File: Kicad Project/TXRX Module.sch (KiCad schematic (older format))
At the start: 16 parts, among them U10 GALI-2+, U11 BandpassFilter, U13 Antenna111, U14 Antenna111, U9 LEE-39+

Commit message: PCB LAYOUT update
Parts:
- gave numbers to parts that had none: 2
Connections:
- net labels added: PowerSplitter, RFIN
- net labels removed: receive_out, transmit_in
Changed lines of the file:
@@
 Text Notes 6500 5800 0    60   ~ 0
 Hello world
-Text HLabel 2350 2650 0    60   Input ~ 0
-transmit_in
-Text HLabel 2350 4800 0    60   Input ~ 0
-receive_out
 $Comp
 L C C11
@@
 $EndComp
 $Comp
-L GND #PWR015
+L GND #PWR011
 U 1 1 59FFE5A2
 P 2350 4350
-F 0 "#PWR015" H 2350 4100 50  0001 C CNN
+F 0 "#PWR011" H 2350 4100 50  0001 C CNN
 F 1 "GND" H 2350 4200 50  0000 C CNN
 F 2 "" H 2350 4350 50  0001 C CNN
@@
 $EndComp
 $Comp
-L GND #PWR016
+L GND #PWR012
 U 1 1 59FFE5D4
 P 3850 5400
-F 0 "#PWR016" H 3850 5150 50  0001 C CNN
+F 0 "#PWR012" H 3850 5150 50  0001 C CNN
 F 1 "GND" H 3850 5250 50  0000 C CNN
 F 2 "" H 3850 5400 50  0001 C CNN
@@
 $EndComp
 $Comp
-L GND #PWR017
+L GND #PWR013
 U 1 1 59FFE606
 P 4050 3200
-F 0 "#PWR017" H 4050 2950 50  0001 C CNN
+F 0 "#PWR013" H 4050 2950 50  0001 C CNN
 F 1 "GND" H 4050 3050 50  0000 C CNN
 F 2 "" H 4050 3200 50  0001 C CNN
@@
 $EndComp
 $Comp
-L GND #PWR018
+L GND #PWR014
 U 1 1 59FFE638
 P 5450 2200
-F 0 "#PWR018" H 5450 1950 50  0001 C CNN
+F 0 "#PWR014" H 5450 1950 50  0001 C CNN
 F 1 "GND" H 5450 2050 50  0000 C CNN
 F 2 "" H 5450 2200 50  0001 C CNN
@@
 	2350 4800 2550 4800
 $Comp
-L +9V #PWR?
+L +9V #PWR015
 U 1 1 5A01141C
 P 5750 1500
-F 0 "#PWR?" H 5750 1350 50  0001 C CNN
+F 0 "#PWR015" H 5750 1350 50  0001 C CNN
 F 1 "+9V" H 5750 1640 50  0000 C CNN
 F 2 "" H 5750 1500 50  0001 C CNN
@@
 $EndComp
 $Comp
-L +9V #PWR?
+L +9V #PWR016
 U 1 1 5A0114D0
 P 3700 3800
-F 0 "#PWR?" H 3700 3650 50  0001 C CNN
+F 0 "#PWR016" H 3700 3650 50  0001 C CNN
 F 1 "+9V" H 3700 3940 50  0000 C CNN
 F 2 "" H 3700 3800 50  0001 C CNN
@@
 	5750 1650 5750 1500
 $Comp
-L BandpassFilterRx U?
+L BandpassFilterRx U3
 U 1 1 5A012078
 P 6700 5750
-F 0 "U?" H 6700 5750 60  0000 C CNN
+F 0 "U3" H 6700 5750 60  0000 C CNN
 F 1 "BandpassFilterRx" H 7250 6100 60  0000 C CNN
 F 2 "" H 6700 5750 60  0001 C CNN
@@
 $EndComp
 $Comp
-L C C?
+L C C4
 U 1 1 5A012959
 P 4800 4800
-F 0 "C?" H 4825 4900 50  0000 L CNN
+F 0 "C4" H 4825 4900 50  0000 L CNN
 F 1 "150p" H 4825 4700 50  0000 L CNN
 F 2 "" H 4838 4650 50  0001 C CNN
@@
 Wire Wire Line
 	4650 4800 4550 4800
+Text GLabel 2350 2650 0    60   Input ~ 0
+PowerSplitter
+Text GLabel 2350 4800 0    60   Input ~ 0
+RFIN
 $EndSCHEMATC

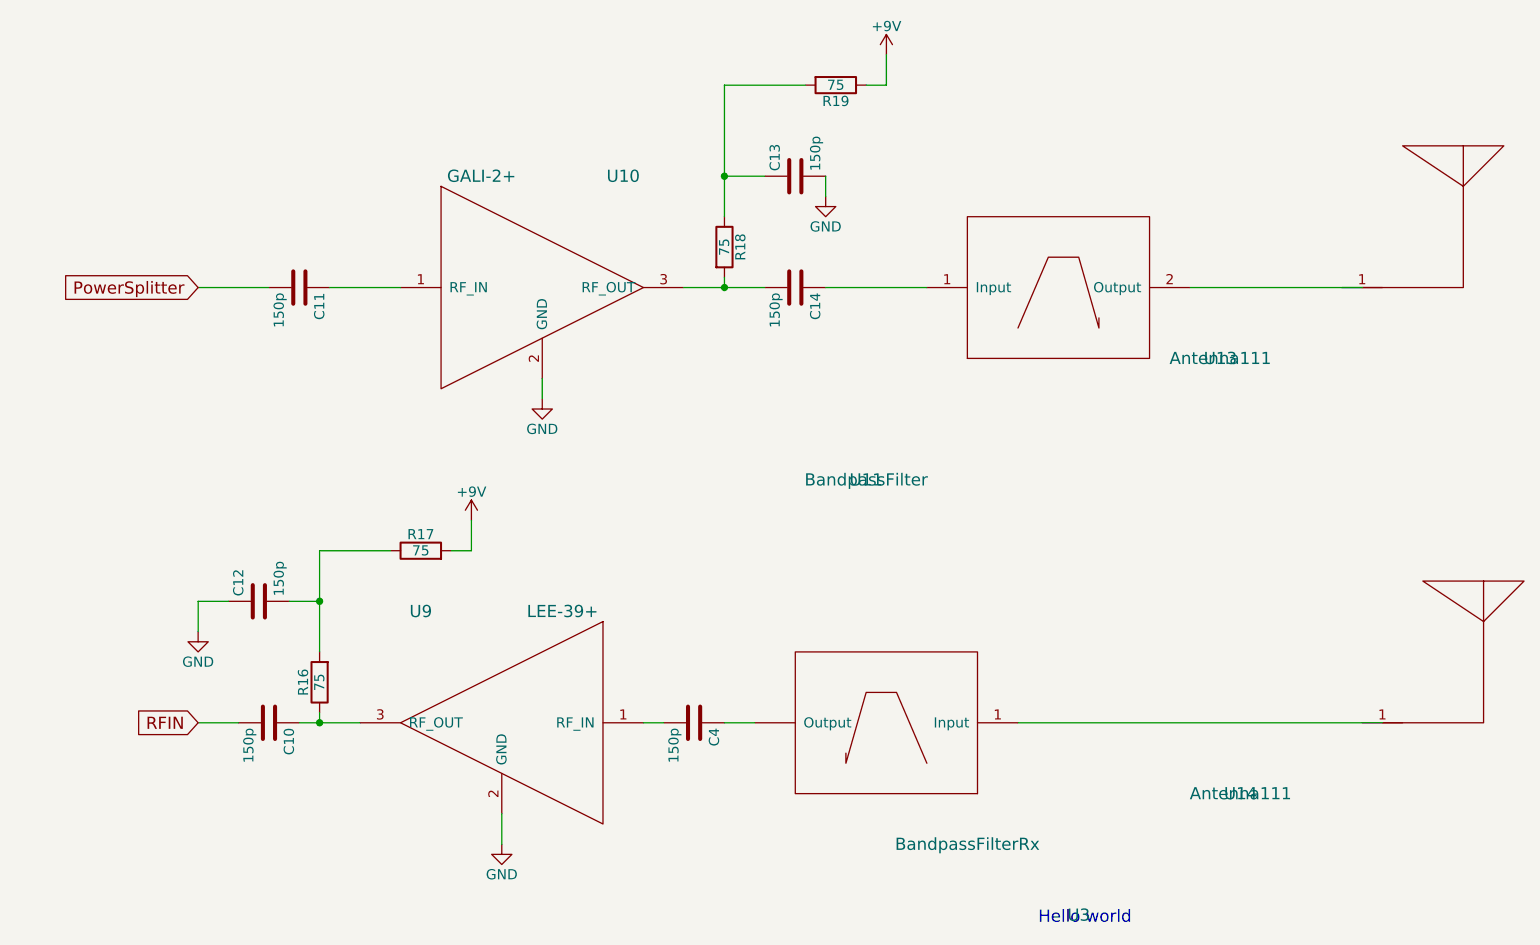
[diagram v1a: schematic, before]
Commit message: Added Filters to PCB
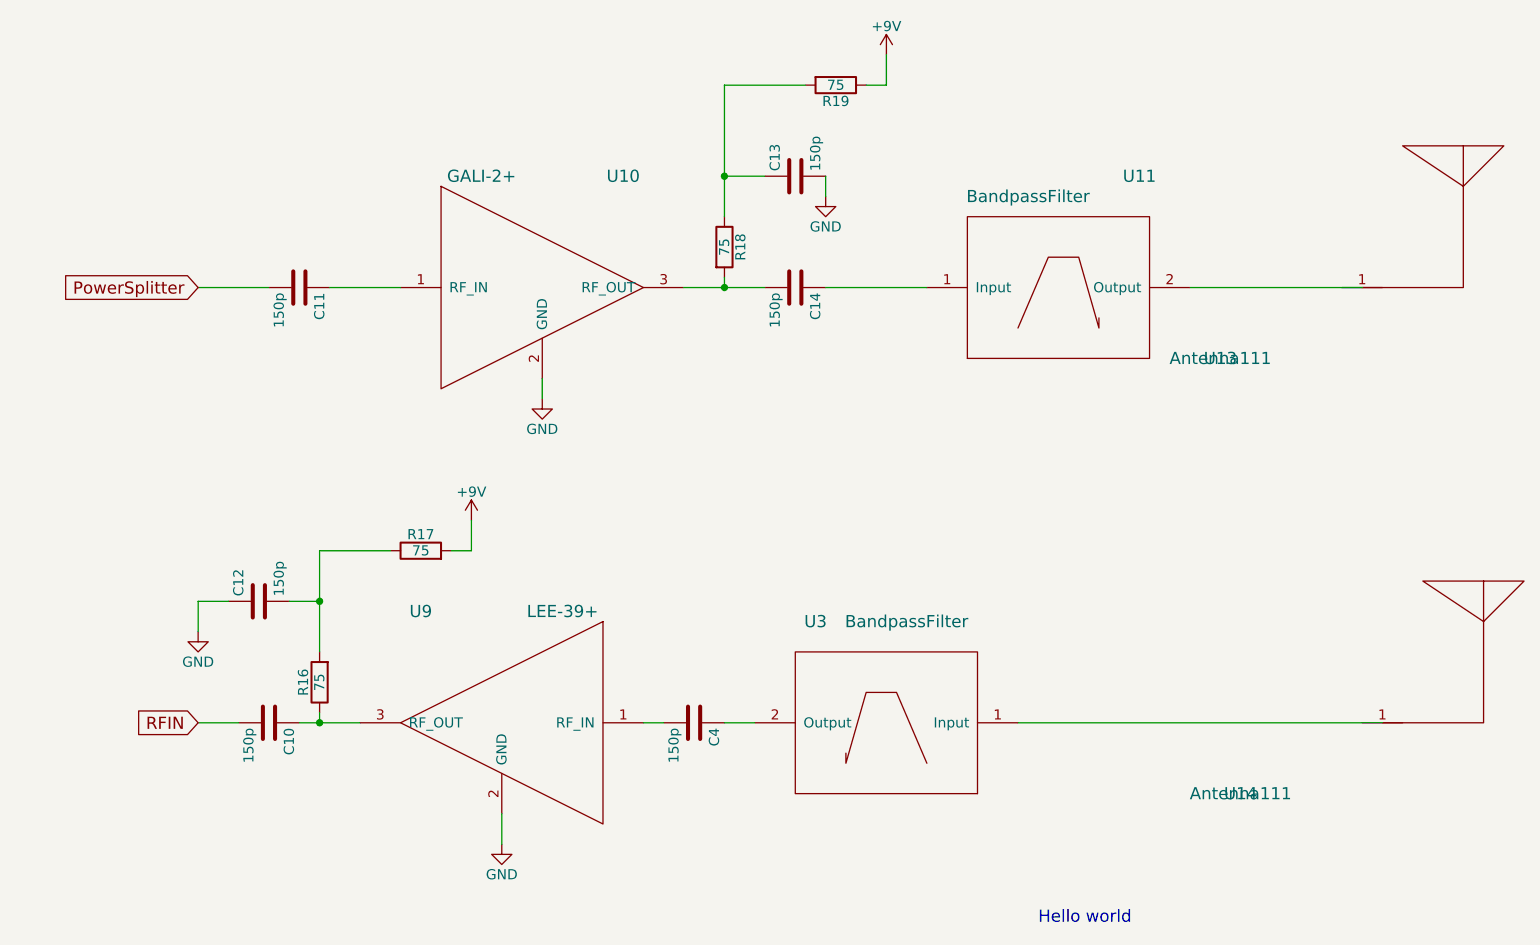
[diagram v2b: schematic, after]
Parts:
- removed U3: BandpassFilterRx, symbol BandpassFilterRx
- added U3: BandpassFilter, RadarComponents:QuadPoleFilter, symbol BandpassFilter
- U11: footprint (none) -> RadarComponents:DoubleFilter
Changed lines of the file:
@@
 U 1 1 59FF71CB
 P 5650 3600
-F 0 "U11" H 5650 3600 60  0000 C CNN
-F 1 "BandpassFilter" H 5650 3600 60  0000 C CNN
-F 2 "" H 5650 3600 60  0001 C CNN
+F 0 "U11" H 7000 5100 60  0000 C CNN
+F 1 "BandpassFilter" H 6450 5000 60  0000 C CNN
+F 2 "RadarComponents:DoubleFilter" H 5650 3600 60  0001 C CNN
 F 3 "" H 5650 3600 60  0001 C CNN
 	1    5650 3600
@@
 	5750 1650 5750 1500
 $Comp
-L BandpassFilterRx U3
-U 1 1 5A012078
-P 6700 5750
-F 0 "U3" H 6700 5750 60  0000 C CNN
-F 1 "BandpassFilterRx" H 7250 6100 60  0000 C CNN
-F 2 "" H 6700 5750 60  0001 C CNN
-F 3 "" H 6700 5750 60  0001 C CNN
-	1    6700 5750
-	-1   0    0    -1
-$EndComp
-$Comp
 L C C4
 U 1 1 5A012959
@@
 Text GLabel 2350 4800 0    60   Input ~ 0
 RFIN
+$Comp
+L BandpassFilter U3
+U 1 1 5A02863C
+P 6700 5750
+F 0 "U3" H 8000 7200 60  0000 C CNN
+F 1 "BandpassFilter" H 7550 7200 60  0000 C CNN
+F 2 "RadarComponents:QuadPoleFilter" H 6700 5750 60  0001 C CNN
+F 3 "" H 6700 5750 60  0001 C CNN
+	1    6700 5750
+	-1   0    0    -1
+$EndComp
 $EndSCHEMATC

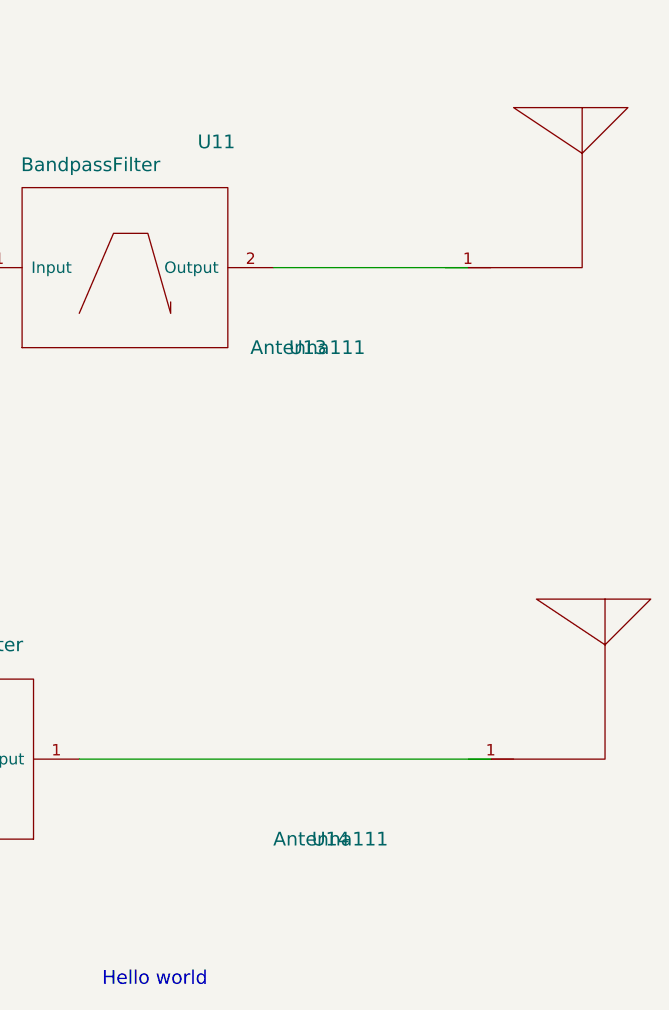
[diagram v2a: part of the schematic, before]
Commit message: added antennas to pcb
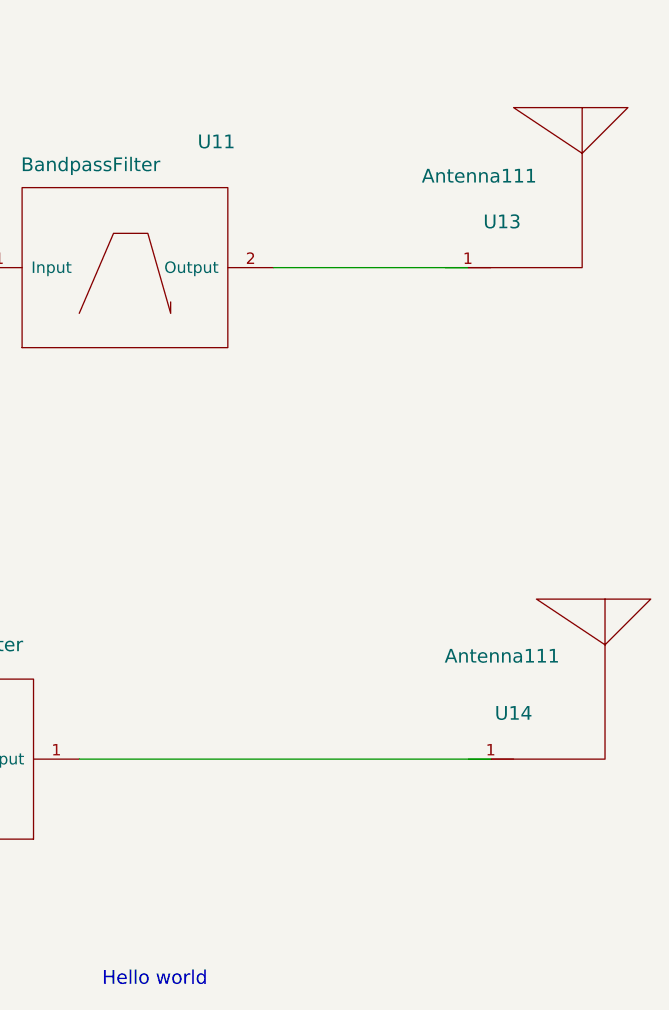
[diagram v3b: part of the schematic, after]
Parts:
- U13, U14: footprint (none) -> RadarComponents:patch58
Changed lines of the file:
@@
 U 1 1 59FFCB61
 P 7400 3000
-F 0 "U13" H 7400 3000 60  0000 C CNN
-F 1 "Antenna111" H 7400 3000 60  0000 C CNN
-F 2 "" H 7400 3000 60  0001 C CNN
+F 0 "U13" H 8250 3550 60  0000 C CNN
+F 1 "Antenna111" H 8150 3750 60  0000 C CNN
+F 2 "RadarComponents:patch58" H 7400 3000 60  0001 C CNN
 F 3 "" H 7400 3000 60  0001 C CNN
 	1    7400 3000
@@
 U 1 1 59FFCBF8
 P 7500 5150
-F 0 "U14" H 7500 5150 60  0000 C CNN
-F 1 "Antenna111" H 7500 5150 60  0000 C CNN
-F 2 "" H 7500 5150 60  0001 C CNN
+F 0 "U14" H 8300 5700 60  0000 C CNN
+F 1 "Antenna111" H 8250 5950 60  0000 C CNN
+F 2 "RadarComponents:patch58" H 7500 5150 60  0001 C CNN
 F 3 "" H 7500 5150 60  0001 C CNN
 	1    7500 5150
